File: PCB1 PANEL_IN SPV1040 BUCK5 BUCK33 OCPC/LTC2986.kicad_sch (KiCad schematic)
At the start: 9 parts, among them U1 LTC2986HLX-PBF

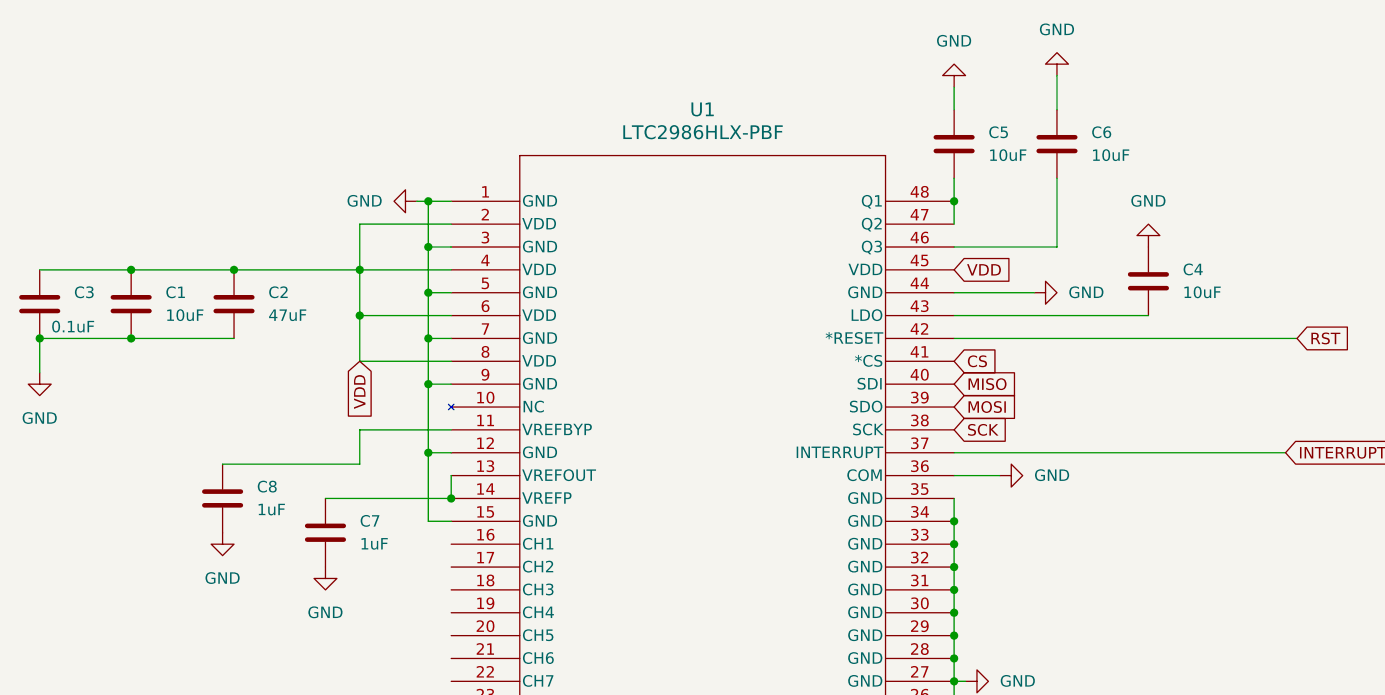
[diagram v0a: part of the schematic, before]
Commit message: Added some comments in POWERPCB, about bus interface
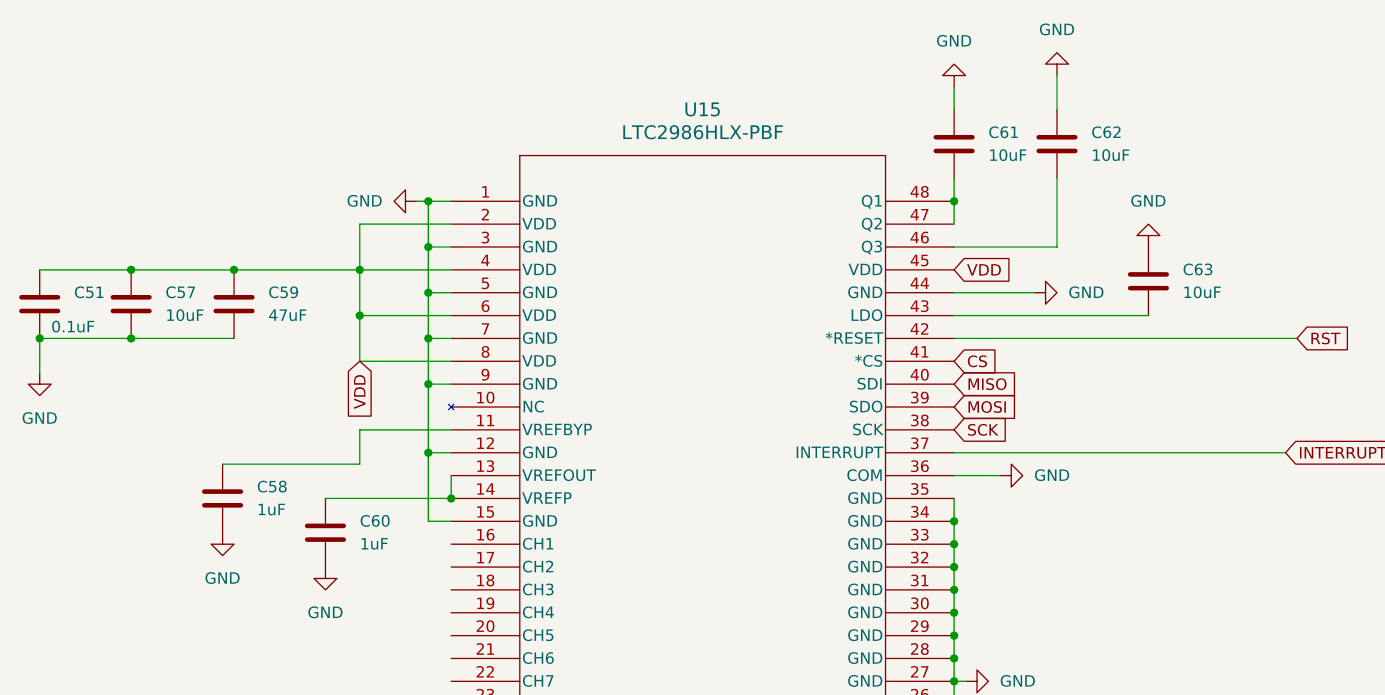
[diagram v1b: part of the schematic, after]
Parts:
- renumbered C3 to C51, C1 to C57, C8 to C58, C2 to C59, C7 to C60, C5 to C61, C6 to C62, C4 to C63, U1 to U15
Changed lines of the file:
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@@
 		(dnp no)
 		(fields_autoplaced yes)
-		(property "Reference" "#PWR01"
+		(property "Reference" "#PWR0111"
 			(at 97.79 38.1 0)
 			(effects
@@
 		)
 		(instances
+			(project "PCB1 PANEL_IN SPV1040 BUCK5 BUCK33 OCPC"
+				(path "/494c9d9f-6b33-4248-a813-27ffaaa929bd/81ba6a5a-e21d-4cec-83f0-5d840c1285ed"
+					(reference "#PWR0111")
+					(unit 1)
+				)
+			)
 			(project ""
 				(path "/e5df9c19-46f5-47d3-b6f4-a0778a1551ae"
@@
 		(dnp no)
 		(fields_autoplaced yes)
-		(property "Reference" "U1"
+		(property "Reference" "U15"
 			(at 135.89 27.94 0)
 			(effects
@@
 		)
 		(instances
+			(project "PCB1 PANEL_IN SPV1040 BUCK5 BUCK33 OCPC"
+				(path "/494c9d9f-6b33-4248-a813-27ffaaa929bd/81ba6a5a-e21d-4cec-83f0-5d840c1285ed"
+					(reference "U15")
+					(unit 1)
+				)
+			)
 			(project ""
 				(path "/e5df9c19-46f5-47d3-b6f4-a0778a1551ae"
@@
 		(dnp no)
 		(fields_autoplaced yes)
-		(property "Reference" "#PWR05"
+		(property "Reference" "#PWR0164"
 			(at 185.42 36.83 0)
 			(effects
@@
 		)
 		(instances
+			(project "PCB1 PANEL_IN SPV1040 BUCK5 BUCK33 OCPC"
+				(path "/494c9d9f-6b33-4248-a813-27ffaaa929bd/81ba6a5a-e21d-4cec-83f0-5d840c1285ed"
+					(reference "#PWR0164")
+					(unit 1)
+				)
+			)
 			(project "LTC2986"
 				(path "/e5df9c19-46f5-47d3-b6f4-a0778a1551ae"
@@
 		(dnp no)
 		(fields_autoplaced yes)
-		(property "Reference" "C6"
+		(property "Reference" "C62"
 			(at 179.07 30.4799 0)
 			(effects
@@
 		)
 		(instances
+			(project "PCB1 PANEL_IN SPV1040 BUCK5 BUCK33 OCPC"
+				(path "/494c9d9f-6b33-4248-a813-27ffaaa929bd/81ba6a5a-e21d-4cec-83f0-5d840c1285ed"
+					(reference "C62")
+					(unit 1)
+				)
+			)
 			(project "LTC2986"
 				(path "/e5df9c19-46f5-47d3-b6f4-a0778a1551ae"
@@
 		(dnp no)
 		(fields_autoplaced yes)
-		(property "Reference" "#PWR04"
+		(property "Reference" "#PWR0159"
 			(at 62.23 63.5 0)
 			(effects
@@
 		)
 		(instances
+			(project "PCB1 PANEL_IN SPV1040 BUCK5 BUCK33 OCPC"
+				(path "/494c9d9f-6b33-4248-a813-27ffaaa929bd/81ba6a5a-e21d-4cec-83f0-5d840c1285ed"
+					(reference "#PWR0159")
+					(unit 1)
+				)
+			)
 			(project "LTC2986"
 				(path "/e5df9c19-46f5-47d3-b6f4-a0778a1551ae"
@@
 		(dnp no)
 		(fields_autoplaced yes)
-		(property "Reference" "C5"
+		(property "Reference" "C61"
 			(at 167.64 30.4799 0)
 			(effects
@@
 		)
 		(instances
+			(project "PCB1 PANEL_IN SPV1040 BUCK5 BUCK33 OCPC"
+				(path "/494c9d9f-6b33-4248-a813-27ffaaa929bd/81ba6a5a-e21d-4cec-83f0-5d840c1285ed"
+					(reference "C61")
+					(unit 1)
+				)
+			)
 			(project "LTC2986"
 				(path "/e5df9c19-46f5-47d3-b6f4-a0778a1551ae"
@@
 		(dnp no)
 		(fields_autoplaced yes)
-		(property "Reference" "C2"
+		(property "Reference" "C59"
 			(at 87.63 48.2599 0)
 			(effects
@@
 		)
 		(instances
+			(project "PCB1 PANEL_IN SPV1040 BUCK5 BUCK33 OCPC"
+				(path "/494c9d9f-6b33-4248-a813-27ffaaa929bd/81ba6a5a-e21d-4cec-83f0-5d840c1285ed"
+					(reference "C59")
+					(unit 1)
+				)
+			)
 			(project "LTC2986"
 				(path "/e5df9c19-46f5-47d3-b6f4-a0778a1551ae"
@@
 		(dnp no)
 		(fields_autoplaced yes)
-		(property "Reference" "C8"
+		(property "Reference" "C58"
 			(at 86.36 69.8499 0)
 			(effects
@@
 		)
 		(instances
+			(project "PCB1 PANEL_IN SPV1040 BUCK5 BUCK33 OCPC"
+				(path "/494c9d9f-6b33-4248-a813-27ffaaa929bd/81ba6a5a-e21d-4cec-83f0-5d840c1285ed"
+					(reference "C58")
+					(unit 1)
+				)
+			)
 			(project "LTC2986"
 				(path "/e5df9c19-46f5-47d3-b6f4-a0778a1551ae"
@@
 		(dnp no)
 		(fields_autoplaced yes)
-		(property "Reference" "#PWR02"
+		(property "Reference" "#PWR0160"
 			(at 171.45 91.44 0)
 			(effects
@@
 		)
 		(instances
+			(project "PCB1 PANEL_IN SPV1040 BUCK5 BUCK33 OCPC"
+				(path "/494c9d9f-6b33-4248-a813-27ffaaa929bd/81ba6a5a-e21d-4cec-83f0-5d840c1285ed"
+					(reference "#PWR0160")
+					(unit 1)
+				)
+			)
 			(project "LTC2986"
 				(path "/e5df9c19-46f5-47d3-b6f4-a0778a1551ae"
@@
 		(dnp no)
 		(fields_autoplaced yes)
-		(property "Reference" "C1"
+		(property "Reference" "C57"
 			(at 76.2 48.2599 0)
 			(effects
@@
 		)
 		(instances
+			(project "PCB1 PANEL_IN SPV1040 BUCK5 BUCK33 OCPC"
+				(path "/494c9d9f-6b33-4248-a813-27ffaaa929bd/81ba6a5a-e21d-4cec-83f0-5d840c1285ed"
+					(reference "C57")
+					(unit 1)
+				)
+			)
 			(project ""
 				(path "/e5df9c19-46f5-47d3-b6f4-a0778a1551ae"
@@
 		(dnp no)
 		(fields_autoplaced yes)
-		(property "Reference" "#PWR03"
+		(property "Reference" "#PWR0165"
 			(at 179.07 48.26 0)
 			(effects
@@
 		)
 		(instances
+			(project "PCB1 PANEL_IN SPV1040 BUCK5 BUCK33 OCPC"
+				(path "/494c9d9f-6b33-4248-a813-27ffaaa929bd/81ba6a5a-e21d-4cec-83f0-5d840c1285ed"
+					(reference "#PWR0165")
+					(unit 1)
+				)
+			)
 			(project "LTC2986"
 				(path "/e5df9c19-46f5-47d3-b6f4-a0778a1551ae"
@@
 		(dnp no)
 		(fields_autoplaced yes)
-		(property "Reference" "C7"
+		(property "Reference" "C60"
 			(at 97.79 73.6599 0)
 			(effects
@@
 		)
 		(instances
+			(project "PCB1 PANEL_IN SPV1040 BUCK5 BUCK33 OCPC"
+				(path "/494c9d9f-6b33-4248-a813-27ffaaa929bd/81ba6a5a-e21d-4cec-83f0-5d840c1285ed"
+					(reference "C60")
+					(unit 1)
+				)
+			)
 			(project "LTC2986"
 				(path "/e5df9c19-46f5-47d3-b6f4-a0778a1551ae"
@@
 		(dnp no)
 		(fields_autoplaced yes)
-		(property "Reference" "#PWR09"
+		(property "Reference" "#PWR0167"
 			(at 93.98 85.09 0)
 			(effects
@@
 		)
 		(instances
+			(project "PCB1 PANEL_IN SPV1040 BUCK5 BUCK33 OCPC"
+				(path "/494c9d9f-6b33-4248-a813-27ffaaa929bd/81ba6a5a-e21d-4cec-83f0-5d840c1285ed"
+					(reference "#PWR0167")
+					(unit 1)
+				)
+			)
 			(project "LTC2986"
 				(path "/e5df9c19-46f5-47d3-b6f4-a0778a1551ae"
@@
 		(dnp no)
 		(fields_autoplaced yes)
-		(property "Reference" "#PWR010"
+		(property "Reference" "#PWR0166"
 			(at 82.55 81.28 0)
 			(effects
@@
 		)
 		(instances
+			(project "PCB1 PANEL_IN SPV1040 BUCK5 BUCK33 OCPC"
+				(path "/494c9d9f-6b33-4248-a813-27ffaaa929bd/81ba6a5a-e21d-4cec-83f0-5d840c1285ed"
+					(reference "#PWR0166")
+					(unit 1)
+				)
+			)
 			(project "LTC2986"
 				(path "/e5df9c19-46f5-47d3-b6f4-a0778a1551ae"
@@
 		(on_board yes)
 		(dnp no)
-		(property "Reference" "C3"
+		(property "Reference" "C51"
 			(at 66.04 48.2599 0)
 			(effects
@@
 		)
 		(instances
+			(project "PCB1 PANEL_IN SPV1040 BUCK5 BUCK33 OCPC"
+				(path "/494c9d9f-6b33-4248-a813-27ffaaa929bd/81ba6a5a-e21d-4cec-83f0-5d840c1285ed"
+					(reference "C51")
+					(unit 1)
+				)
+			)
 			(project "LTC2986"
 				(path "/e5df9c19-46f5-47d3-b6f4-a0778a1551ae"
@@
 		(dnp no)
 		(fields_autoplaced yes)
-		(property "Reference" "#PWR06"
+		(property "Reference" "#PWR0162"
 			(at 163.83 19.05 0)
 			(effects
@@
 		)
 		(instances
+			(project "PCB1 PANEL_IN SPV1040 BUCK5 BUCK33 OCPC"
+				(path "/494c9d9f-6b33-4248-a813-27ffaaa929bd/81ba6a5a-e21d-4cec-83f0-5d840c1285ed"
+					(reference "#PWR0162")
+					(unit 1)
+				)
+			)
 			(project "LTC2986"
 				(path "/e5df9c19-46f5-47d3-b6f4-a0778a1551ae"
@@
 		(dnp no)
 		(fields_autoplaced yes)
-		(property "Reference" "C4"
+		(property "Reference" "C63"
 			(at 189.23 45.7199 0)
 			(effects
@@
 		)
 		(instances
+			(project "PCB1 PANEL_IN SPV1040 BUCK5 BUCK33 OCPC"
+				(path "/494c9d9f-6b33-4248-a813-27ffaaa929bd/81ba6a5a-e21d-4cec-83f0-5d840c1285ed"
+					(reference "C63")
+					(unit 1)
+				)
+			)
 			(project "LTC2986"
 				(path "/e5df9c19-46f5-47d3-b6f4-a0778a1551ae"
@@
 		(dnp no)
 		(fields_autoplaced yes)
-		(property "Reference" "#PWR07"
+		(property "Reference" "#PWR0163"
 			(at 175.26 17.78 0)
 			(effects
@@
 		)
 		(instances
+			(project "PCB1 PANEL_IN SPV1040 BUCK5 BUCK33 OCPC"
+				(path "/494c9d9f-6b33-4248-a813-27ffaaa929bd/81ba6a5a-e21d-4cec-83f0-5d840c1285ed"
+					(reference "#PWR0163")
+					(unit 1)
+				)
+			)
 			(project "LTC2986"
 				(path "/e5df9c19-46f5-47d3-b6f4-a0778a1551ae"
@@
 		(dnp no)
 		(fields_autoplaced yes)
-		(property "Reference" "#PWR08"
+		(property "Reference" "#PWR0161"
 			(at 175.26 68.58 0)
 			(effects
@@
 		)
 		(instances
-			(project "LTC2986"
-				(path "/e5df9c19-46f5-47d3-b6f4-a0778a1551ae"
+			(project "PCB1 PANEL_IN SPV1040 BUCK5 BUCK33 OCPC"
+				(path "/494c9d9f-6b33-4248-a813-27ffaaa929bd/81ba6a5a-e21d-4cec-83f0-5d840c1285ed"
+					(reference "#PWR0161")
+					(unit 1)
+				)
+			)
+			(project "LTC2986"
+				(path "/e5df9c19-46f5-47d3-b6f4-a0778a1551ae"
